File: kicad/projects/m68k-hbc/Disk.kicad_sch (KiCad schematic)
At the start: 11 parts, among them J14 IDC_PATA, J15 IDC_FDD, U30 PC8477BV, Y3 24M

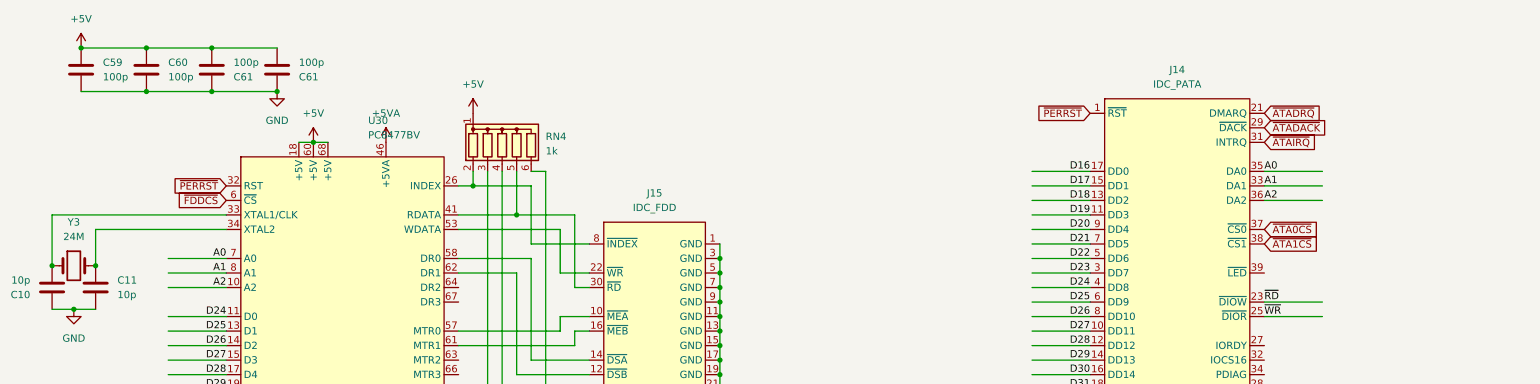
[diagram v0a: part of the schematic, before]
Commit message: Modified system architecture, New KiCad Project: Cache Memory Module(SIMM80)
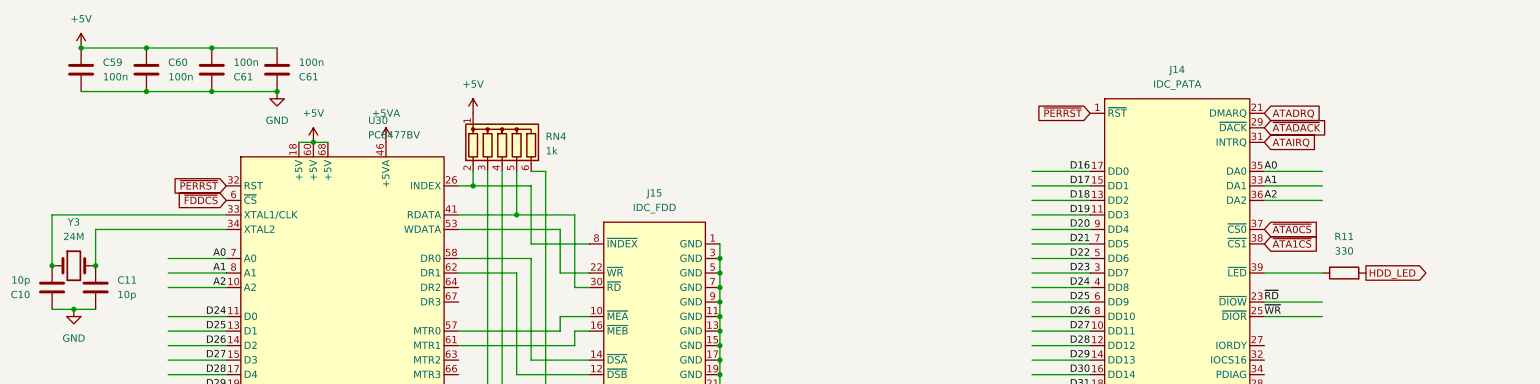
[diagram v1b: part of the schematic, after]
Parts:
- added R11: 330, Resistor_SMD:R_1206_3216Metric_Pad1.30x1.75mm_HandSolder, symbol Device:R
- C59, C60, C61: value 100p -> 100n
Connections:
- net at J14.39 (~{LED}): now also R11.1
- net ~{ATADRQ} renamed ATADRQ
- net ~{ATAIRQ} renamed ATAIRQ
- new net HDD_LED: R11.2
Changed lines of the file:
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@@
+    (stroke (width 0) (type default))
+  )
+  (wire (pts (xy 254 80.01) (xy 243.84 80.01))
     (stroke (width 0) (type default))
   )
@@
     )
   )
+  (global_label "HDD_LED" (shape output) (at 261.62 80.01 0) (fields_autoplaced)
+    (effects (font (size 1.27 1.27)) (justify left))
+    (property "Intersheetrefs" "${INTERSHEET_REFS}" (at 272.811 80.01 0)
+      (effects (font (size 1.27 1.27)) (justify left) hide)
+    )
+  )
   (global_label "SIZ[0..1]" (shape output) (at 262.89 140.97 0) (fields_autoplaced)
     (effects (font (size 1.27 1.27)) (justify left))
@@
     )
   )
-  (global_label "~{ATADRQ}" (shape input) (at 243.84 52.07 0) (fields_autoplaced)
+  (global_label "ATADRQ" (shape input) (at 243.84 52.07 0) (fields_autoplaced)
     (effects (font (size 1.27 1.27)) (justify left))
     (property "Intersheetrefs" "${INTERSHEET_REFS}" (at 253.7611 52.07 0)
@@
     )
   )
-  (global_label "~{ATAIRQ}" (shape input) (at 243.84 57.15 0) (fields_autoplaced)
+  (global_label "ATAIRQ" (shape input) (at 243.84 57.15 0) (fields_autoplaced)
     (effects (font (size 1.27 1.27)) (justify left))
     (property "Intersheetrefs" "${INTERSHEET_REFS}" (at 253.0959 57.15 0)
@@
         )
         (path "/da427610-5b61-43bd-a536-c238ace8bf3f/cefc2d69-725a-46c9-93bb-98595beffb09"
-          (reference "Y4") (unit 1)
+          (reference "Y2") (unit 1)
         )
       )
@@
         )
         (path "/da427610-5b61-43bd-a536-c238ace8bf3f/cefc2d69-725a-46c9-93bb-98595beffb09"
-          (reference "#PWR0177") (unit 1)
+          (reference "#PWR0122") (unit 1)
         )
       )
@@
         )
         (path "/da427610-5b61-43bd-a536-c238ace8bf3f/cefc2d69-725a-46c9-93bb-98595beffb09"
-          (reference "#PWR0176") (unit 1)
+          (reference "#PWR0121") (unit 1)
         )
       )
@@
         )
         (path "/da427610-5b61-43bd-a536-c238ace8bf3f/cefc2d69-725a-46c9-93bb-98595beffb09"
-          (reference "C51") (unit 1)
+          (reference "C35") (unit 1)
         )
       )
@@
         )
         (path "/da427610-5b61-43bd-a536-c238ace8bf3f/cefc2d69-725a-46c9-93bb-98595beffb09"
-          (reference "U22") (unit 1)
+          (reference "U6") (unit 1)
         )
       )
@@
         )
         (path "/da427610-5b61-43bd-a536-c238ace8bf3f/cefc2d69-725a-46c9-93bb-98595beffb09"
-          (reference "J13") (unit 1)
+          (reference "J12") (unit 1)
         )
       )
@@
         )
         (path "/da427610-5b61-43bd-a536-c238ace8bf3f/cefc2d69-725a-46c9-93bb-98595beffb09"
-          (reference "RN7") (unit 1)
+          (reference "RN2") (unit 1)
         )
       )
@@
         )
         (path "/da427610-5b61-43bd-a536-c238ace8bf3f/cefc2d69-725a-46c9-93bb-98595beffb09"
-          (reference "C52") (unit 1)
+          (reference "C36") (unit 1)
+        )
+      )
+    )
+  )
+  (symbol (lib_id "Device:R") (at 257.81 80.01 90) (unit 1)
+    (in_bom yes) (on_board yes) (dnp no) (fields_autoplaced)
+    (property "Reference" "R11" (at 257.81 73.66 90)
+      (effects (font (size 1.27 1.27)))
+    )
+    (property "Value" "330" (at 257.81 76.2 90)
+      (effects (font (size 1.27 1.27)))
+    )
+    (property "Footprint" "Resistor_SMD:R_1206_3216Metric_Pad1.30x1.75mm_HandSolder" (at 257.81 81.788 90)
+      (effects (font (size 1.27 1.27)) hide)
+    )
+    (property "Datasheet" "~" (at 257.81 80.01 0)
+      (effects (font (size 1.27 1.27)) hide)
+    )
+    (pin "1")
+    (pin "2")
+    (instances
+      (project "m68k-hbc"
+        (path "/da427610-5b61-43bd-a536-c238ace8bf3f/2b5df2c4-3183-4e1c-a9e9-17fef73528cf"
+          (reference "R11") (unit 1)
+        )
+        (path "/da427610-5b61-43bd-a536-c238ace8bf3f/cefc2d69-725a-46c9-93bb-98595beffb09"
+          (reference "R4") (unit 1)
         )
       )
@@
         )
         (path "/da427610-5b61-43bd-a536-c238ace8bf3f/cefc2d69-725a-46c9-93bb-98595beffb09"
-          (reference "#PWR0179") (unit 1)
+          (reference "#PWR0124") (unit 1)
         )
       )
@@
         )
         (path "/da427610-5b61-43bd-a536-c238ace8bf3f/cefc2d69-725a-46c9-93bb-98595beffb09"
-          (reference "J14") (unit 1)
+          (reference "J13") (unit 1)
         )
       )
@@
       (effects (font (size 1.27 1.27)) (justify left))
     )
-    (property "Value" "100p" (at 63.5 43.18 0)
+    (property "Value" "100n" (at 63.5 43.18 0)
       (effects (font (size 1.27 1.27)) (justify left))
     )
@@
         )
         (path "/da427610-5b61-43bd-a536-c238ace8bf3f/cefc2d69-725a-46c9-93bb-98595beffb09"
-          (reference "C49") (unit 1)
+          (reference "C33") (unit 1)
         )
       )
@@
         )
         (path "/da427610-5b61-43bd-a536-c238ace8bf3f/cefc2d69-725a-46c9-93bb-98595beffb09"
-          (reference "#PWR0175") (unit 1)
+          (reference "#PWR0120") (unit 1)
         )
       )
@@
         )
         (path "/da427610-5b61-43bd-a536-c238ace8bf3f/cefc2d69-725a-46c9-93bb-98595beffb09"
-          (reference "#PWR0170") (unit 1)
+          (reference "#PWR0115") (unit 1)
         )
       )
@@
       (effects (font (size 1.27 1.27)) (justify left))
     )
-    (property "Value" "100p" (at 52.07 45.72 0)
+    (property "Value" "100n" (at 52.07 45.72 0)
       (effects (font (size 1.27 1.27)) (justify left))
     )
@@
         )
         (path "/da427610-5b61-43bd-a536-c238ace8bf3f/cefc2d69-725a-46c9-93bb-98595beffb09"
-          (reference "C48") (unit 1)
+          (reference "C32") (unit 1)
         )
       )
@@
         )
         (path "/da427610-5b61-43bd-a536-c238ace8bf3f/cefc2d69-725a-46c9-93bb-98595beffb09"
-          (reference "#PWR0171") (unit 1)
+          (reference "#PWR0116") (unit 1)
         )
       )
@@
       (effects (font (size 1.27 1.27)) (justify left))
     )
-    (property "Value" "100p" (at 74.93 43.18 0)
+    (property "Value" "100n" (at 74.93 43.18 0)
       (effects (font (size 1.27 1.27)) (justify left))
     )
@@
         )
         (path "/da427610-5b61-43bd-a536-c238ace8bf3f/cefc2d69-725a-46c9-93bb-98595beffb09"
-          (reference "C50") (unit 1)
+          (reference "C34") (unit 1)
         )
       )
@@
         )
         (path "/da427610-5b61-43bd-a536-c238ace8bf3f/cefc2d69-725a-46c9-93bb-98595beffb09"
-          (reference "#PWR0173") (unit 1)
+          (reference "#PWR0118") (unit 1)
         )
       )
@@
         )
         (path "/da427610-5b61-43bd-a536-c238ace8bf3f/cefc2d69-725a-46c9-93bb-98595beffb09"
-          (reference "#PWR0180") (unit 1)
+          (reference "#PWR0125") (unit 1)
         )
       )
@@
         )
         (path "/da427610-5b61-43bd-a536-c238ace8bf3f/cefc2d69-725a-46c9-93bb-98595beffb09"
-          (reference "#PWR0172") (unit 1)
+          (reference "#PWR0117") (unit 1)
         )
       )
@@
         )
         (path "/da427610-5b61-43bd-a536-c238ace8bf3f/cefc2d69-725a-46c9-93bb-98595beffb09"
-          (reference "#PWR0178") (unit 1)
+          (reference "#PWR0123") (unit 1)
         )
       )
@@
       (effects (font (size 1.27 1.27)) (justify left))
     )
-    (property "Value" "100p" (at 40.64 45.72 0)
+    (property "Value" "100n" (at 40.64 45.72 0)
       (effects (font (size 1.27 1.27)) (justify left))
     )
@@
         )
         (path "/da427610-5b61-43bd-a536-c238ace8bf3f/cefc2d69-725a-46c9-93bb-98595beffb09"
-          (reference "C47") (unit 1)
+          (reference "C31") (unit 1)
         )
       )
@@
         )
         (path "/da427610-5b61-43bd-a536-c238ace8bf3f/cefc2d69-725a-46c9-93bb-98595beffb09"
-          (reference "#PWR0181") (unit 1)
+          (reference "#PWR0126") (unit 1)
         )
       )
@@
         )
         (path "/da427610-5b61-43bd-a536-c238ace8bf3f/cefc2d69-725a-46c9-93bb-98595beffb09"
-          (reference "#PWR0174") (unit 1)
-        )
-      )
+          (reference "#PWR0119") (unit 1)
+        )
+      )

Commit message: Some Updates
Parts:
- removed C10, C11: 10p, Capacitor_SMD:C_1206_3216Metric_Pad1.33x1.80mm_HandSolder, symbol Device:C
- removed C59, C60, C61 (x2): 100n, Capacitor_SMD:C_1206_3216Metric_Pad1.33x1.80mm_HandSolder, symbol Device:C
- removed J15: IDC_FDD, Connector_IDC:IDC-Header_2x17_P2.54mm_Vertical, symbol IDC_SpecialPurpose:IDC_FDD
- removed RN4: 1k, Resistor_THT:R_Array_SIP6, symbol Device:R_Network05
- removed U30: PC8477BV, Package_LCC:PLCC-68_THT-Socket, symbol PC8477BV:PC8477BV
- removed Y3: 24M, Crystal:Crystal_HC52-6mm_Vertical, symbol Device:Crystal
- R11: value 330 -> R; footprint Resistor_SMD:R_1206_3216Metric_Pad1.30x1.75mm_HandSolder -> Resistor_SMD:R_0603_1608Metric_Pad0.98x0.95mm_HandSolder
- renumbered J14 to J?
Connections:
- net ATA_IORDY/~{ATA_DDRDY}/ATA_DDSTR: now reaches J?.27 (IORDY)
- net ~{ATA_PDIAG}/~{ATA_CBLID}: now reaches J?.34 (PDIAG)
- net A0 renamed ATA_A0
- net A1 renamed ATA_A1
- net A2 renamed ATA_A2
- net ATADRQ renamed ATA_DRQ
- net ATAIRQ renamed ATA_IRQ
- net D16 renamed ATA_D0
- net D17 renamed ATA_D1
- net D18 renamed ATA_D2
- net D19 renamed ATA_D3
- net D20 renamed ATA_D4
- net D21 renamed ATA_D5
- net D22 renamed ATA_D6
- net D23 renamed ATA_D7
- net D24 renamed ATA_D8
- net D25 renamed ATA_D9
- net D26 renamed ATA_D10
- net D27 renamed ATA_D11
- net D28 renamed ATA_D12
- net D29 renamed ATA_D13
- net D30 renamed ATA_D14
- net D31 renamed ATA_D15
- net HDD_LED renamed LED_HDD
- net ~{ATA0CS} renamed ~{CS_ATA0}
- net ~{ATA1CS} renamed ~{CS_ATA1}
- net ~{ATADACK} renamed ~{ATA_DACK}
- net ~{PERRST} renamed ~{RST_ATA}
- net ~{RD} renamed ~{ATA_IOR}/~{ATA_HDRDY}/ATA_HDSTR
- net ~{WR} renamed ~{ATA_IOW}/STOP
- no-connect marks 11 -> 0
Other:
- note added: "ATA Signals"
- moved on the sheet: J?, R11
